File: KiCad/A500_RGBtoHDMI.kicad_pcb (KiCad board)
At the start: 2 copper layers, 80 x 30 mm, 3 parts, among them J1 Conn_02x20_Odd_Even, U1 Denise_MB_pins, U2 Denise_SocketOnAdapter

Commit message: improved design
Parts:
- U1: value Denise_MB_pins -> Denise_MB_PinHeader
- U2: value Denise_SocketOnAdapter -> Denise_MB_PinSocket
- moved U1 71.5 mm to (188.0, 88.1), turned to 270 degrees
- moved U2 71.5 mm to (188.0, 77.7), turned to 270 degrees
- moved J1 17.1 mm to (149.9, 97.4)
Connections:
- U1 pad 1: Net-(U1-Pad1) -> D6
- U1 pad 2: Net-(U1-Pad2) -> D5
- U1 pad 3: Net-(U1-Pad3) -> D4
- U1 pad 4: Net-(U1-Pad4) -> D3
- U1 pad 5: Net-(U1-Pad5) -> D2
- U1 pad 6: Net-(U1-Pad6) -> D1
- U1 pad 7: Net-(U1-Pad7) -> D0
- U2 pad 1: Net-(U2-Pad1) -> D6
- U2 pad 2: Net-(U2-Pad2) -> D5
- U2 pad 3: Net-(U2-Pad3) -> D4
- U2 pad 4: Net-(U2-Pad4) -> D3
- U2 pad 5: Net-(U2-Pad5) -> D2
- U2 pad 6: Net-(U2-Pad6) -> D1
- U2 pad 7: Net-(U2-Pad7) -> D0
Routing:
- net D6: track 0.00 -> 10.4 mm
- net D5: track 0.00 -> 10.4 mm
- net D4: track 0.00 -> 10.4 mm
- net D3: track 0.00 -> 10.4 mm
- net D2: track 0.00 -> 10.4 mm
- net D1: track 0.00 -> 10.4 mm
- net D0: track 0.00 -> 10.4 mm
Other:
- board size 80 x 30 mm -> 80 x 29.5 mm

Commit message: more routing
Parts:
- U2: value Denise_MB_PinSocket -> Denise_Socket
- moved J1 1.27 mm to (148.6, 97.4)
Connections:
- J1 pad 1: VCC -> Net-(J1-Pad1)
- J1 pad 2: GND -> Net-(J1-Pad2)
- U1 pad 10: Net-(U1-Pad10) -> RGA8
- U1 pad 11: Net-(U1-Pad11) -> RGA7
- U1 pad 12: Net-(U1-Pad12) -> RGA6
- U1 pad 13: Net-(U1-Pad13) -> RGA5
- U1 pad 14: Net-(U1-Pad14) -> RGA4
- U1 pad 15: Net-(U1-Pad15) -> RGA3
- U1 pad 16: Net-(U1-Pad16) -> RGA2
- U1 pad 17: Net-(U1-Pad17) -> RGA1
- U1 pad 18: Net-(U1-Pad18) -> BURST
- U1 pad 19: Net-(U1-Pad19) -> VCC
- U1 pad 20: Net-(U1-Pad20) -> R0
- U1 pad 21: Net-(U1-Pad21) -> R1
- U1 pad 22: Net-(U1-Pad22) -> R2
- U1 pad 23: Net-(U1-Pad23) -> R3
- U1 pad 24: Net-(U1-Pad24) -> B0
- U1 pad 25: Net-(U1-Pad25) -> B1
- U1 pad 26: Net-(U1-Pad26) -> B2
- U1 pad 27: Net-(U1-Pad27) -> B3
- U1 pad 28: Net-(U1-Pad28) -> G0
- U1 pad 29: Net-(U1-Pad29) -> G1
- U1 pad 30: Net-(U1-Pad30) -> G2
- U1 pad 31: Net-(U1-Pad31) -> G3
- U1 pad 32: Net-(U1-Pad32) -> CBL
- U1 pad 33: Net-(U1-Pad33) -> ZD
- U1 pad 34: Net-(U1-Pad34) -> CDAC
- U1 pad 35: Net-(U1-Pad35) -> C7M
- U1 pad 36: Net-(U1-Pad36) -> CCK
- U1 pad 37: Net-(U1-Pad37) -> GND
- U1 pad 38: Net-(U1-Pad38) -> M0V
- U1 pad 39: Net-(U1-Pad39) -> M1V
- U1 pad 40: Net-(U1-Pad40) -> D15
- U1 pad 41: Net-(U1-Pad41) -> D14
- U1 pad 42: Net-(U1-Pad42) -> D13
- U1 pad 43: Net-(U1-Pad43) -> D12
- U1 pad 44: Net-(U1-Pad44) -> D11
- U1 pad 45: Net-(U1-Pad45) -> D10
- U1 pad 46: Net-(U1-Pad46) -> D9
- U1 pad 47: Net-(U1-Pad47) -> D8
- U1 pad 48: Net-(U1-Pad48) -> D7
- U1 pad 8: Net-(U1-Pad8) -> M1H
- U1 pad 9: Net-(U1-Pad9) -> M0H
- U2 pad 10: Net-(U2-Pad10) -> RGA8
- U2 pad 11: Net-(U2-Pad11) -> RGA7
- U2 pad 12: Net-(U2-Pad12) -> RGA6
- U2 pad 13: Net-(U2-Pad13) -> RGA5
- U2 pad 14: Net-(U2-Pad14) -> RGA4
- U2 pad 15: Net-(U2-Pad15) -> RGA3
- U2 pad 16: Net-(U2-Pad16) -> RGA2
- U2 pad 17: Net-(U2-Pad17) -> RGA1
- U2 pad 18: Net-(U2-Pad18) -> BURST
- U2 pad 19: Net-(U2-Pad19) -> VCC
- U2 pad 20: Net-(U2-Pad20) -> R0
- U2 pad 21: Net-(U2-Pad21) -> R1
- U2 pad 22: Net-(U2-Pad22) -> R2
- U2 pad 23: Net-(U2-Pad23) -> R3
- U2 pad 24: Net-(U2-Pad24) -> B0
- U2 pad 25: Net-(U2-Pad25) -> B1
- U2 pad 26: Net-(U2-Pad26) -> B2
- U2 pad 27: Net-(U2-Pad27) -> B3
- U2 pad 28: Net-(U2-Pad28) -> G0
- U2 pad 29: Net-(U2-Pad29) -> G1
- U2 pad 30: Net-(U2-Pad30) -> G2
- U2 pad 31: Net-(U2-Pad31) -> G3
- U2 pad 32: Net-(U2-Pad32) -> CBL
- U2 pad 33: Net-(U2-Pad33) -> ZD
- U2 pad 34: Net-(U2-Pad34) -> CDAC
- U2 pad 35: Net-(U2-Pad35) -> C7M
- U2 pad 36: Net-(U2-Pad36) -> CCK
- U2 pad 37: Net-(U2-Pad37) -> GND
- U2 pad 38: Net-(U2-Pad38) -> M0V
- U2 pad 39: Net-(U2-Pad39) -> M1V
- U2 pad 40: Net-(U2-Pad40) -> D15
- U2 pad 41: Net-(U2-Pad41) -> D14
- U2 pad 42: Net-(U2-Pad42) -> D13
- U2 pad 43: Net-(U2-Pad43) -> D12
- U2 pad 44: Net-(U2-Pad44) -> D11
- U2 pad 45: Net-(U2-Pad45) -> D10
- U2 pad 46: Net-(U2-Pad46) -> D9
- U2 pad 47: Net-(U2-Pad47) -> D8
- U2 pad 48: Net-(U2-Pad48) -> D7
- U2 pad 8: Net-(U2-Pad8) -> M1H
- U2 pad 9: Net-(U2-Pad9) -> M0H
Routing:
- net ZD: track 0.00 -> 10.4 mm
- net VCC: track 0.00 -> 10.4 mm
- net RGA8: track 0.00 -> 10.4 mm
- net RGA7: track 0.00 -> 10.4 mm
- net RGA6: track 0.00 -> 10.4 mm
- net RGA5: track 0.00 -> 10.4 mm
- net RGA4: track 0.00 -> 10.4 mm
- net RGA3: track 0.00 -> 10.4 mm
- net RGA2: track 0.00 -> 10.4 mm
- net RGA1: track 0.00 -> 10.4 mm
- net R3: track 0.00 -> 10.4 mm
- net R2: track 0.00 -> 10.4 mm
- net R1: track 0.00 -> 10.4 mm
- net R0: track 0.00 -> 10.4 mm
- net M1V: track 0.00 -> 10.4 mm
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
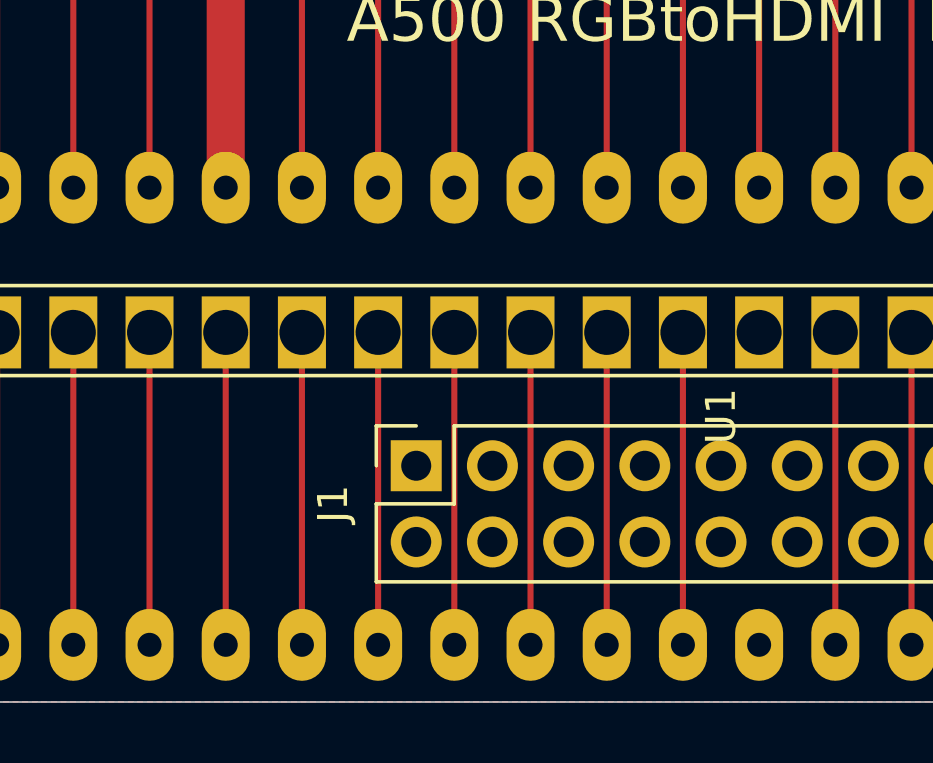
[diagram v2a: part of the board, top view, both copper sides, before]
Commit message: added networks to Pi-header
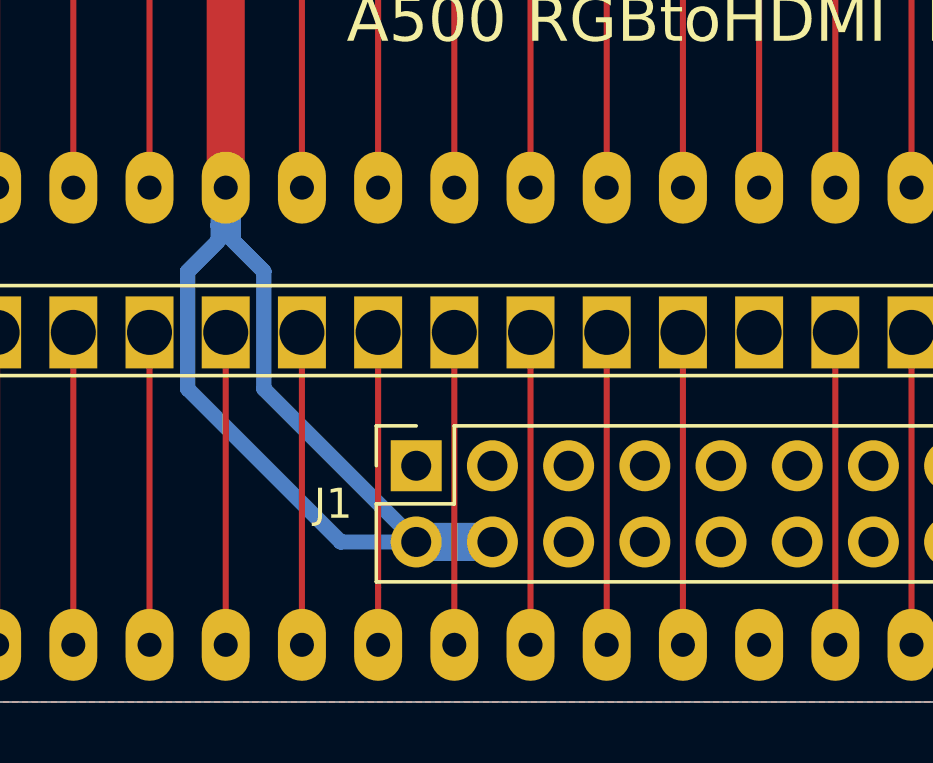
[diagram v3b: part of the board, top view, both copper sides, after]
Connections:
- net Net-(J1-Pad10) renamed GPIO15
- net Net-(J1-Pad11) renamed GPIO17
- net Net-(J1-Pad12) renamed GPIO18
- net Net-(J1-Pad13) renamed GPIO27
- net Net-(J1-Pad15) renamed GPIO22
- net Net-(J1-Pad16) renamed GPIO23
- net Net-(J1-Pad18) renamed GPIO24
- net Net-(J1-Pad19) renamed GPIO10
- net Net-(J1-Pad21) renamed GPIO9
- net Net-(J1-Pad22) renamed GPIO25
- net Net-(J1-Pad23) renamed GPIO11
- net Net-(J1-Pad24) renamed GPIO8
- net Net-(J1-Pad26) renamed GPIO7
- net Net-(J1-Pad27) renamed GPIO0
- net Net-(J1-Pad28) renamed GPIO1
- net Net-(J1-Pad29) renamed GPIO5
- net Net-(J1-Pad3) renamed GPIO2
- net Net-(J1-Pad31) renamed GPIO6
- net Net-(J1-Pad32) renamed GPIO12
- net Net-(J1-Pad33) renamed GPIO13
- net Net-(J1-Pad35) renamed GPIO19
- net Net-(J1-Pad36) renamed GPIO16
- net Net-(J1-Pad37) renamed GPIO26
- net Net-(J1-Pad38) renamed GPIO20
- net Net-(J1-Pad40) renamed GPIO21
- net Net-(J1-Pad5) renamed GPIO3
- net Net-(J1-Pad7) renamed GPIO4
- net Net-(J1-Pad8) renamed GPIO14
- J1 pad 1: Net-(J1-Pad1) -> 3V3
- J1 pad 14: Net-(J1-Pad14) -> GND
- J1 pad 17: Net-(J1-Pad17) -> 3V3
- J1 pad 2: Net-(J1-Pad2) -> VCC
- J1 pad 20: Net-(J1-Pad20) -> GND
- J1 pad 25: Net-(J1-Pad25) -> GND
- J1 pad 30: Net-(J1-Pad30) -> GND
- J1 pad 34: Net-(J1-Pad34) -> GND
- J1 pad 39: Net-(J1-Pad39) -> GND
- J1 pad 4: Net-(J1-Pad4) -> VCC
- J1 pad 6: Net-(J1-Pad6) -> GND
- J1 pad 9: Net-(J1-Pad9) -> GND
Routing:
- net VCC: track 10.4 -> 48.7 mm

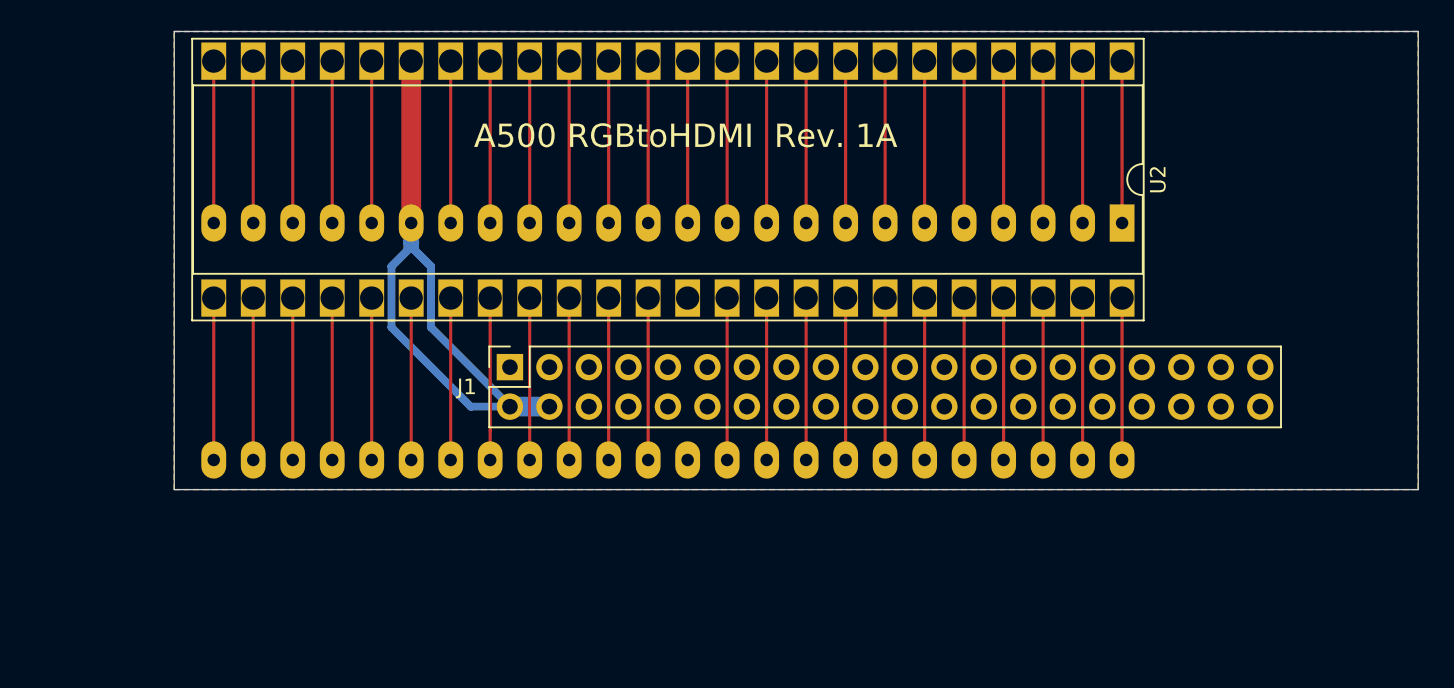
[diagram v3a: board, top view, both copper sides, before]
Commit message: added CPLD XC9572XL-VQ64 and did more layout and routing
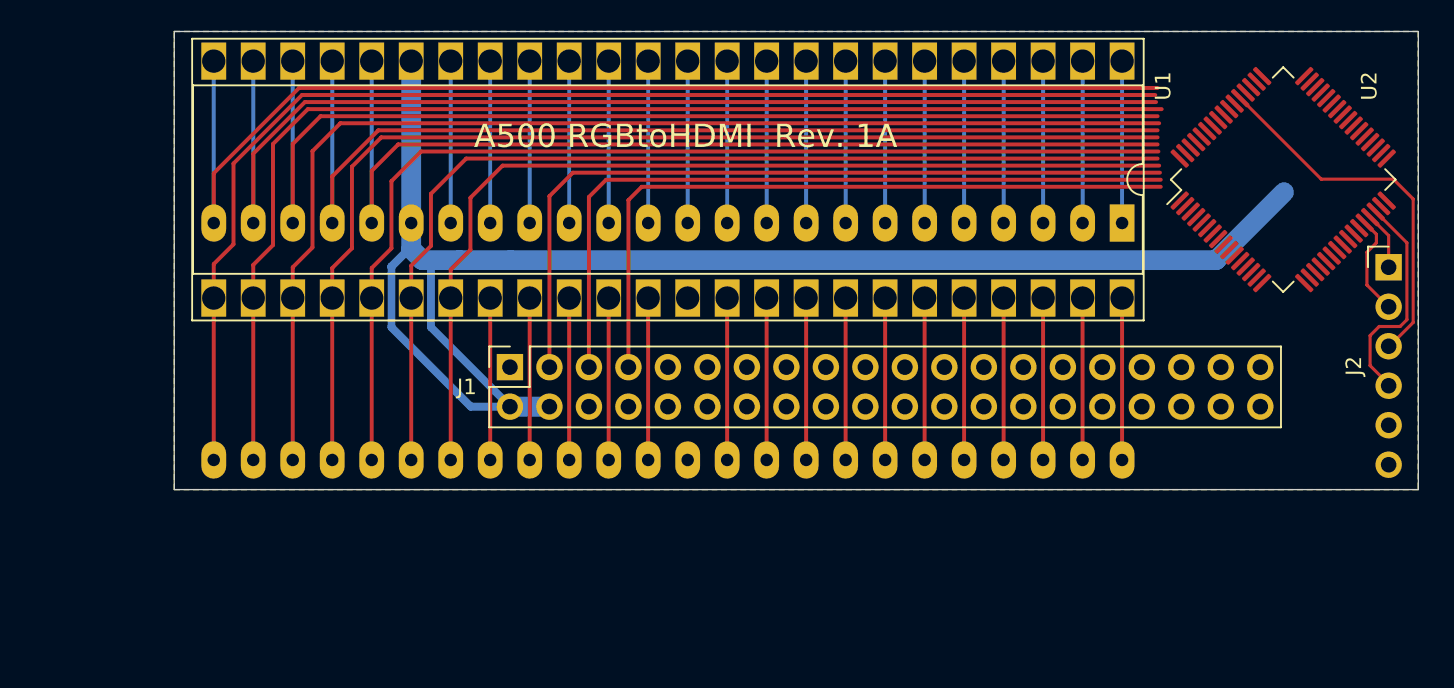
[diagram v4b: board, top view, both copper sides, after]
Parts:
- added J2: Conn_01x06, Connector_PinHeader_2.54mm:PinHeader_1x06_P2.54mm_Vertical, F.Cu at (205.1, 91.0)
- added U2: XC9572XL-VQ64, Package_QFP:TQFP-64_10x10mm_P0.5mm, F.Cu at (198.3, 85.3)
- renumbered U2 to U1, U1 to U3
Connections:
- J1 pad 1: 3V3 -> Net-(J1-Pad1)
- J1 pad 17: 3V3 -> Net-(J1-Pad17)
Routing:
- net B1: track 10.4 -> 80.7 mm
- net B2: track 10.4 -> 78.9 mm
- net B0: track 10.4 -> 76.6 mm
- net B3: track 10.4 -> 75.6 mm
- net R3: track 10.4 -> 74.3 mm
- net G0: track 10.4 -> 72.0 mm
- net R2: track 10.4 -> 71.9 mm
- net VCC: track 48.7 -> 108.6 mm
- net G1: track 10.4 -> 68.6 mm
- net R1: track 10.4 -> 67.7 mm
- net G2: track 10.4 -> 65.3 mm
- net R0: track 10.4 -> 65.0 mm
- net G3: track 10.4 -> 62.5 mm
- net GPIO2: track 0.00 -> 50.9 mm
- net GPIO3: track 0.00 -> 48.2 mm
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
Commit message: more routing and fixes
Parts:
- moved U2 0.85 mm to (199.0, 84.8)
- moved J1 0.63 mm to (148.6, 98.0)
- renumbered J2 to JTAG1
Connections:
- net GPIO0 renamed Net-(J1-Pad27)
- net GPIO1 renamed Net-(J1-Pad28)
- net GPIO14 renamed Net-(J1-Pad8)
- net GPIO15 renamed Net-(J1-Pad10)
- net GPIO16 renamed Net-(J1-Pad36)
- net GPIO19 renamed Net-(J1-Pad35)
- net GPIO22 renamed Net-(J1-Pad15)
- net GPIO24 renamed Net-(J1-Pad18)
- net GPIO25 renamed Net-(J1-Pad22)
- net GPIO26 renamed Net-(J1-Pad37)
- net GPIO27 renamed Net-(J1-Pad13)
- net ZD renamed PIXELSW
- J1 pad 11: GPIO17 -> PSYNC
- J1 pad 12: GPIO18 -> VERSION
- J1 pad 16: GPIO23 -> CSYNC_3V3
- J1 pad 19: GPIO10 -> R0_3V3
- J1 pad 21: GPIO9 -> G3_3V3
- J1 pad 23: GPIO11 -> R1_3V3
- J1 pad 24: GPIO8 -> G2_3V3
- J1 pad 26: GPIO7 -> G1_3V3
- J1 pad 29: GPIO5 -> B3_3V3
- J1 pad 3: GPIO2 -> B0_3V3
- J1 pad 31: GPIO6 -> G0_3V3
- J1 pad 32: GPIO12 -> R2_3V3
- J1 pad 33: GPIO13 -> R3_3V3
- J1 pad 38: GPIO20 -> SPCLK
- J1 pad 40: GPIO21 -> CLK
- J1 pad 5: GPIO3 -> B1_3V3
- J1 pad 7: GPIO4 -> B2_3V3
- U1 pad 32: CBL -> CSYNC
- U2 pad 1: Net-(U2-Pad1) -> B0_3V3
- U2 pad 10: Net-(U2-Pad10) -> B3_3V3
- U2 pad 11: Net-(U2-Pad11) -> G0_3V3
- U2 pad 12: Net-(U2-Pad12) -> G2_3V3
- U2 pad 13: Net-(U2-Pad13) -> G1_3V3
- U2 pad 15: Net-(U2-Pad15) -> CLK
- U2 pad 16: Net-(U2-Pad16) -> SPCLK
- U2 pad 17: Net-(U2-Pad17) -> CSYNC
- U2 pad 18: Net-(U2-Pad18) -> R2_3V3
- U2 pad 19: Net-(U2-Pad19) -> R3_3V3
- U2 pad 2: Net-(U2-Pad2) -> B1_3V3
- U2 pad 4: Net-(U2-Pad4) -> B2_3V3
- U2 pad 49: Net-(U2-Pad49) -> R0
- U2 pad 5: Net-(U2-Pad5) -> PSYNC
- U2 pad 50: Net-(U2-Pad50) -> R1
- U2 pad 51: Net-(U2-Pad51) -> R2
- U2 pad 52: Net-(U2-Pad52) -> R3
- U2 pad 56: Net-(U2-Pad56) -> B0
- U2 pad 57: Net-(U2-Pad57) -> B1
- U2 pad 58: Net-(U2-Pad58) -> B2
- U2 pad 59: Net-(U2-Pad59) -> B3
- U2 pad 6: Net-(U2-Pad6) -> CSYNC_3V3
- U2 pad 60: Net-(U2-Pad60) -> G0
- U2 pad 61: Net-(U2-Pad61) -> G1
- U2 pad 62: Net-(U2-Pad62) -> G2
- U2 pad 63: Net-(U2-Pad63) -> G3
- U2 pad 64: Net-(U2-Pad64) -> VERSION
- U2 pad 7: Net-(U2-Pad7) -> R0_3V3
- U2 pad 8: Net-(U2-Pad8) -> G3_3V3
- U2 pad 9: Net-(U2-Pad9) -> R1_3V3
- U3 pad 32: CBL -> CSYNC
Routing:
- net CSYNC: track 0.00 -> 72.7 mm
- net B0_3V3: track 0.00 -> 54.4 mm
- net B1_3V3: track 0.00 -> 52.1 mm
- net GPIO2: track 50.9 -> 0.00 mm
- net B2_3V3: track 0.00 -> 50.0 mm
- net GPIO3: track 48.2 -> 0.00 mm
- net GPIO4: track 45.3 -> 0.00 mm
- net VERSION: track 0.00 -> 45.1 mm, vias 0 -> 1
- net PSYNC: track 0.00 -> 45.0 mm
- net CSYNC_3V3: track 0.00 -> 36.7 mm, vias 0 -> 1
- net R0_3V3: track 0.00 -> 31.3 mm
- net G3_3V3: track 0.00 -> 28.9 mm
- net G2_3V3: track 0.00 -> 28.8 mm, vias 0 -> 1
- net R1_3V3: track 0.00 -> 26.4 mm
- net 3V3: track 0.00 -> 24.6 mm
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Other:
- net class Default: clearance 0.2 -> 0.2032; trace_width 0.25 -> 0.2032
- rule trace_clearance: 0.2 -> 0.2032
- rule trace_min: 0.2 -> 0.1524
- rule via_min_size: 0.4 -> 0.5

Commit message: more routing and small adjustments,fixes and improvements
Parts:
- moved JTAG1 12.1 mm to (204.9, 103.1), turned to 180 degrees
- moved U2 0.51 mm to (199.0, 84.3)
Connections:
- net PSYNC renamed Pi_CLK
- J1 pad 18: Net-(J1-Pad18) -> TDO
- J1 pad 27: Net-(J1-Pad27) -> TDI_SPDATA
- J1 pad 28: Net-(J1-Pad28) -> TMS_CLKEN
- J1 pad 38: SPCLK -> TCK_SPCLK
- JTAG1 pad 1: TMS -> TMS_CLKEN
- JTAG1 pad 2: TDI -> TDI_SPDATA
- JTAG1 pad 4: TCK -> TCK_SPCLK
- U2 pad 16: SPCLK -> TCK_SPCLK
- U2 pad 27: Net-(U2-Pad27) -> TDI_SPDATA
- U2 pad 28: TDI -> TDI_SPDATA
- U2 pad 29: TMS -> TMS_CLKEN
- U2 pad 30: TCK -> TCK_SPCLK
- U2 pad 31: Net-(U2-Pad31) -> TMS_CLKEN
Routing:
- net TMS_CLKEN: track 0.00 -> 60.8 mm
- net TDO: track 23.9 -> 75.1 mm
- net TDI_SPDATA: track 0.00 -> 50.8 mm
- net TCK_SPCLK: track 0.00 -> 48.3 mm
- net 3V3: track 24.6 -> 0.00 mm
- net TCK: track 14.7 -> 0.00 mm
- net SPCLK: track 12.9 -> 0.00 mm
- net TDI: track 7.36 -> 0.00 mm
- net TMS: track 4.26 -> 0.00 mm
- net R0: track 71.6 -> 69.9 mm
- net VERSION: track 45.1 -> 45.7 mm
- net R3_3V3: track 17.6 -> 18.1 mm
- net GND: vias 0 -> 4
